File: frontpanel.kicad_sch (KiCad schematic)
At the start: 16 parts, among them J1 CV, J10 1x4 m, J12 1x6 m, J14 1x2 m, J16 1x6 m, J2 FM, J3 SAW, J4 PWM, J5 PUL, J6 TRI, J8 1x9 m

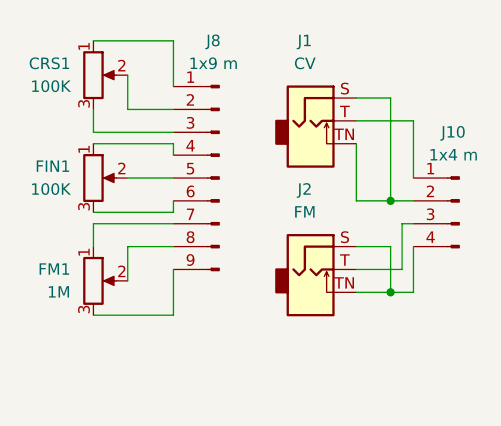
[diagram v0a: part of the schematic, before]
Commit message: Fixed inverted pots
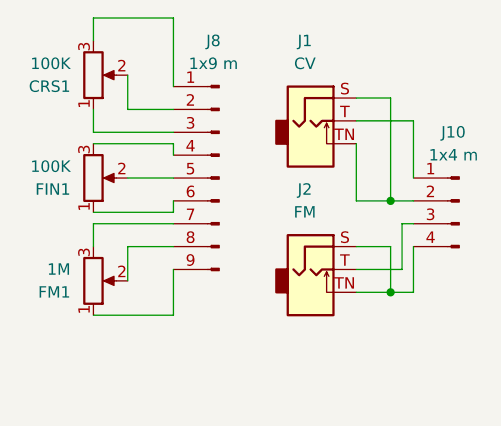
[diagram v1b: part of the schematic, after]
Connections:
- net at FIN1.1: now also J8.6 (Pin_6); no longer J8.4 (Pin_4)
- net at FIN1.3: now also J8.4 (Pin_4); no longer J8.6 (Pin_6)
- net at CRS1.1: now also J8.3 (Pin_3); no longer J8.1 (Pin_1)
- net at CRS1.3: now also J8.1 (Pin_1); no longer J8.3 (Pin_3)
- net at J8.7 (Pin_7): now also FM1.3; no longer FM1.1
- net at J8.9 (Pin_9): now also FM1.1; no longer FM1.3
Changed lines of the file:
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@@
+	(wire
+		(pts
+			(xy 24.13 17.78) (xy 24.13 20.32)
+		)
+		(stroke
+			(width 0)
+			(type default)
+		)
+	)
 	(wire
 		(pts
@@
 	(wire
 		(pts
-			(xy 24.13 20.32) (xy 33.02 20.32)
+			(xy 24.13 17.78) (xy 33.02 17.78)
 		)
 		(stroke
@@
 	(wire
 		(pts
-			(xy 33.02 20.32) (xy 33.02 25.4)
+			(xy 33.02 17.78) (xy 33.02 25.4)
 		)
 		(stroke
@@
 		(lib_id "Device:R_Potentiometer")
 		(at 24.13 35.56 0)
+		(mirror x)
 		(unit 1)
 		(exclude_from_sim no)
@@
 		(on_board yes)
 		(dnp no)
-		(fields_autoplaced yes)
 		(property "Reference" "FIN1"
-			(at 21.59 34.2899 0)
+			(at 21.59 36.8301 0)
 			(effects
 				(font
@@
 		)
 		(property "Value" "100K"
-			(at 21.59 36.8299 0)
+			(at 21.59 34.2901 0)
 			(effects
 				(font
@@
 		(lib_id "Device:R_Potentiometer")
 		(at 24.13 24.13 0)
+		(mirror x)
 		(unit 1)
 		(exclude_from_sim no)
@@
 		(on_board yes)
 		(dnp no)
-		(fields_autoplaced yes)
 		(property "Reference" "CRS1"
-			(at 21.59 22.8599 0)
+			(at 21.59 25.4001 0)
 			(effects
 				(font
@@
 		)
 		(property "Value" "100K"
-			(at 21.59 25.3999 0)
+			(at 21.59 22.8601 0)
 			(effects
 				(font
@@
 		(lib_id "Device:R_Potentiometer")
 		(at 24.13 46.99 0)
+		(mirror x)
 		(unit 1)
 		(exclude_from_sim no)
@@
 		(on_board yes)
 		(dnp no)
-		(fields_autoplaced yes)
 		(property "Reference" "FM1"
-			(at 21.59 45.7199 0)
+			(at 21.59 48.2601 0)
 			(effects
 				(font
@@
 		)
 		(property "Value" "1M"
-			(at 21.59 48.2599 0)
-			(effects
-				(font
+			(at 21.59 45.7201 0)
+			(effects
+				(font
